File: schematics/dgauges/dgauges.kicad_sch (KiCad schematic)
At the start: 19 parts, among them J1 Conn_01x05_Female, U1 74HC595, U2 74HC595, U3 74HC595, U4 74HC595, U5 74HC595

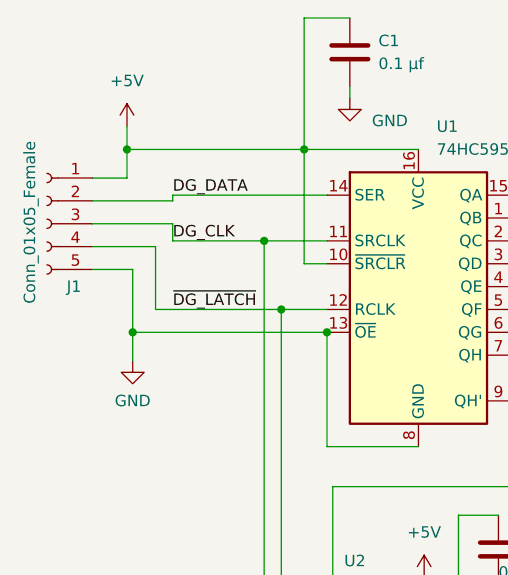
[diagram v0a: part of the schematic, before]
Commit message: SCH: dgauge => ust proper JST connector for J1
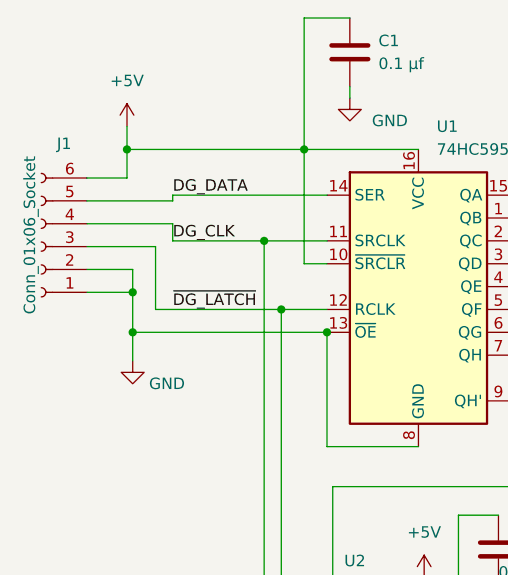
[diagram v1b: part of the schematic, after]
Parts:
- removed J1: Conn_01x05_Female, Connectors_JST:JST_EH_B05B-EH-A_05x2.50mm_Straight, symbol Connector:Conn_01x05_Female
- added J1: Conn_01x06_Socket, Connector_JST:JST_PH_B6B-PH-K_1x06_P2.00mm_Vertical, symbol Connector:Conn_01x06_Socket
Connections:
- net +5V: now also J1.6 (Pin_6)
- net DG_CLK: now also J1.4 (Pin_4)
- net DG_DATA: now also J1.5 (Pin_5)
- net GND: now also J1.1 (Pin_1), J1.2 (Pin_2)
- net ~{DG_LATCH}: now also J1.3 (Pin_3)

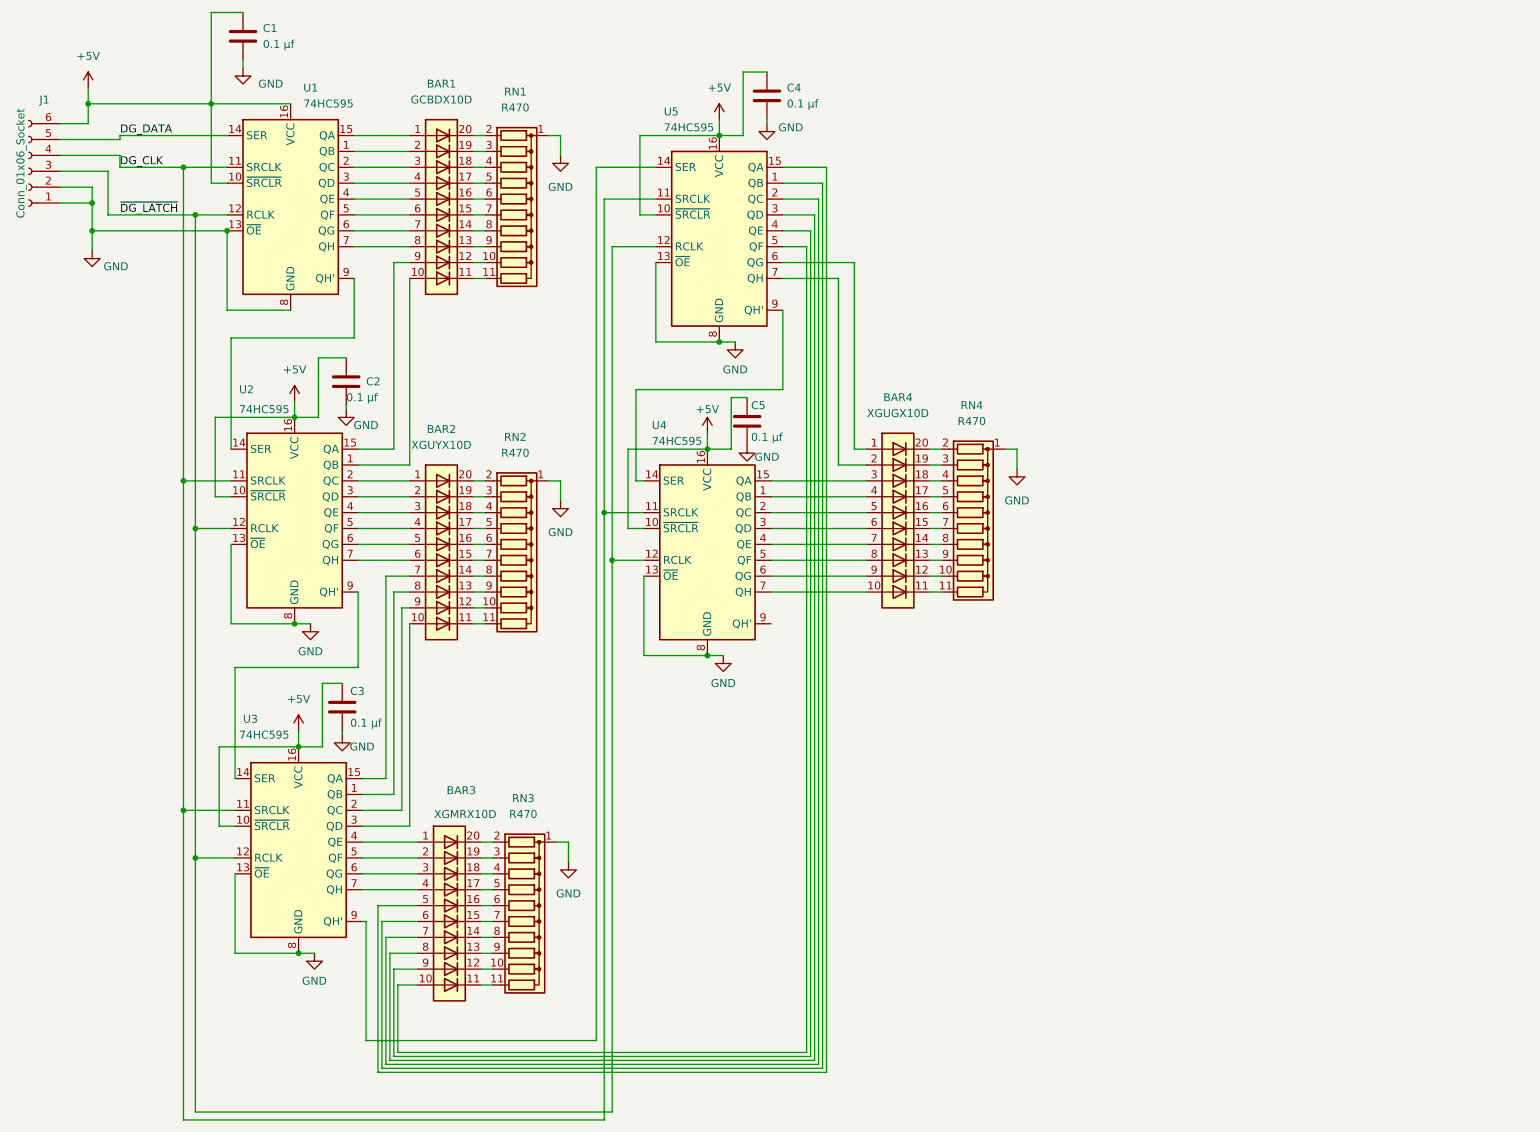
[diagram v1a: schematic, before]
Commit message: SCH: DGauges: route serial out to header for daisy-chaining
And add mounting holes
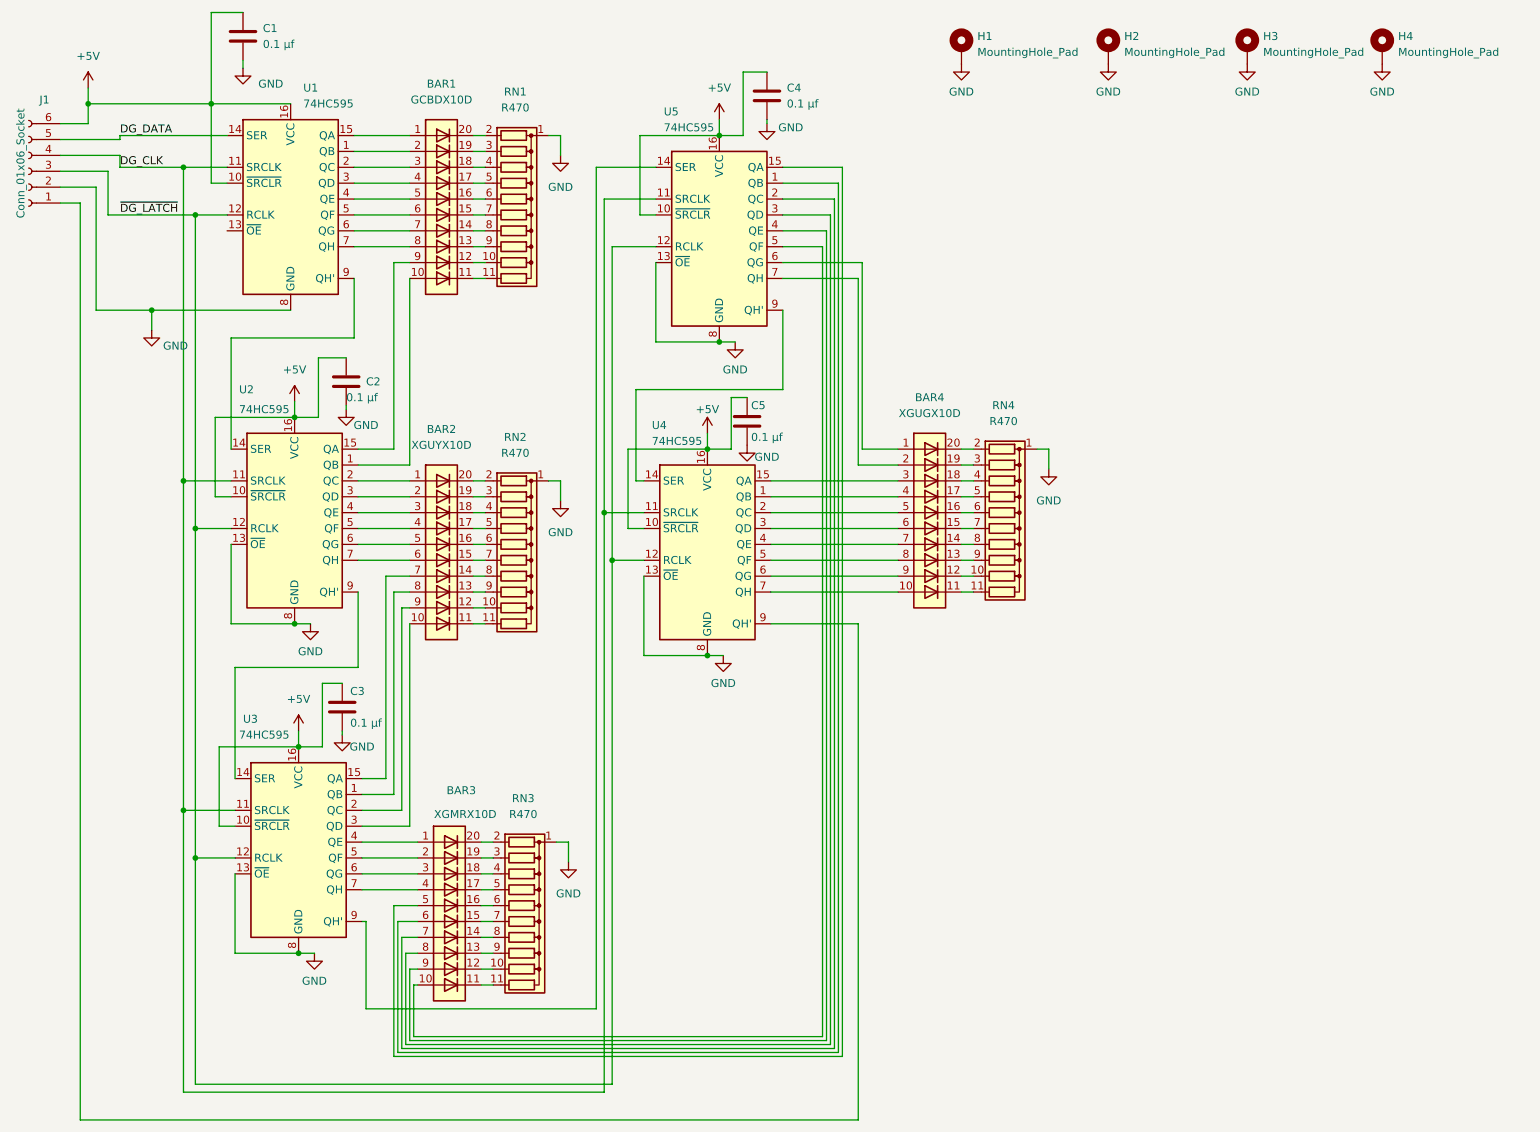
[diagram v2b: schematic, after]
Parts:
- added H1, H2, H3, H4: MountingHole_Pad, MountingHole:MountingHole_2.2mm_M2_ISO7380_Pad, symbol Mechanical:MountingHole_Pad
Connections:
- net GND: now also H1.1, H2.1, H3.1, H4.1; no longer J1.1 (Pin_1), U1.13 (~{OE})
- net at U4.9 (QH'): now also J1.1 (Pin_1)
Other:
- moved on the sheet: BAR4, RN4

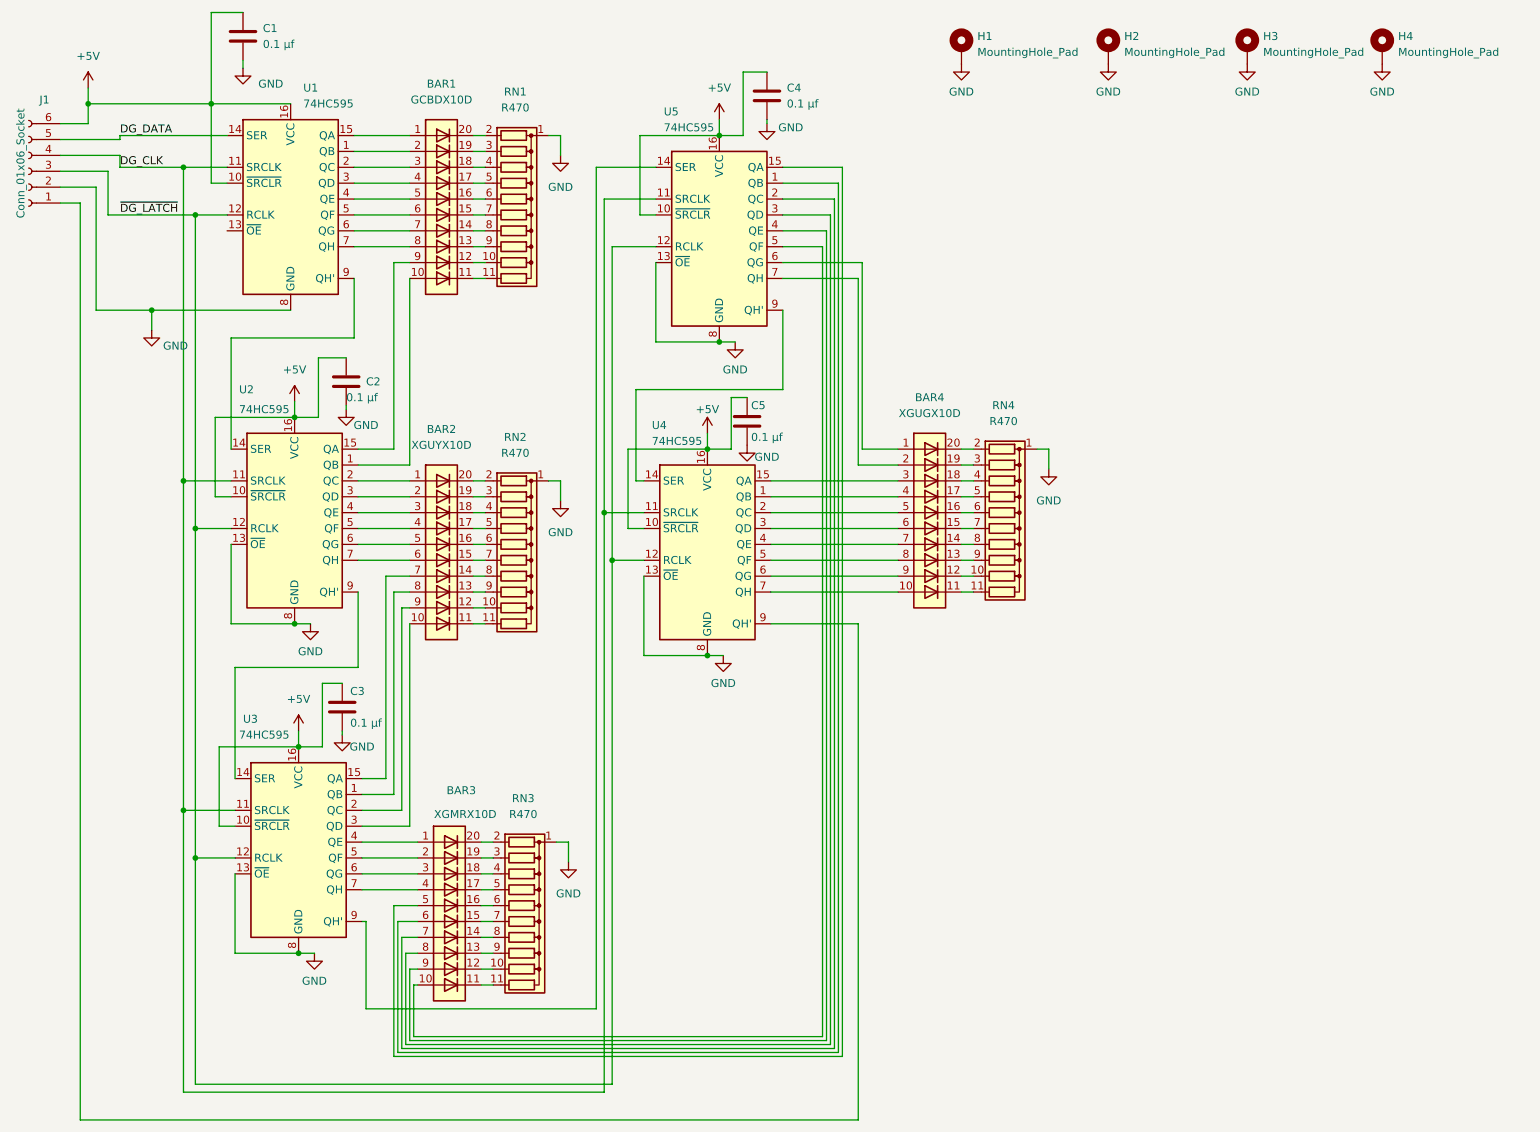
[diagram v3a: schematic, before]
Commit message: SCH: dgauges=> set res. values to get similar brightness on all bars
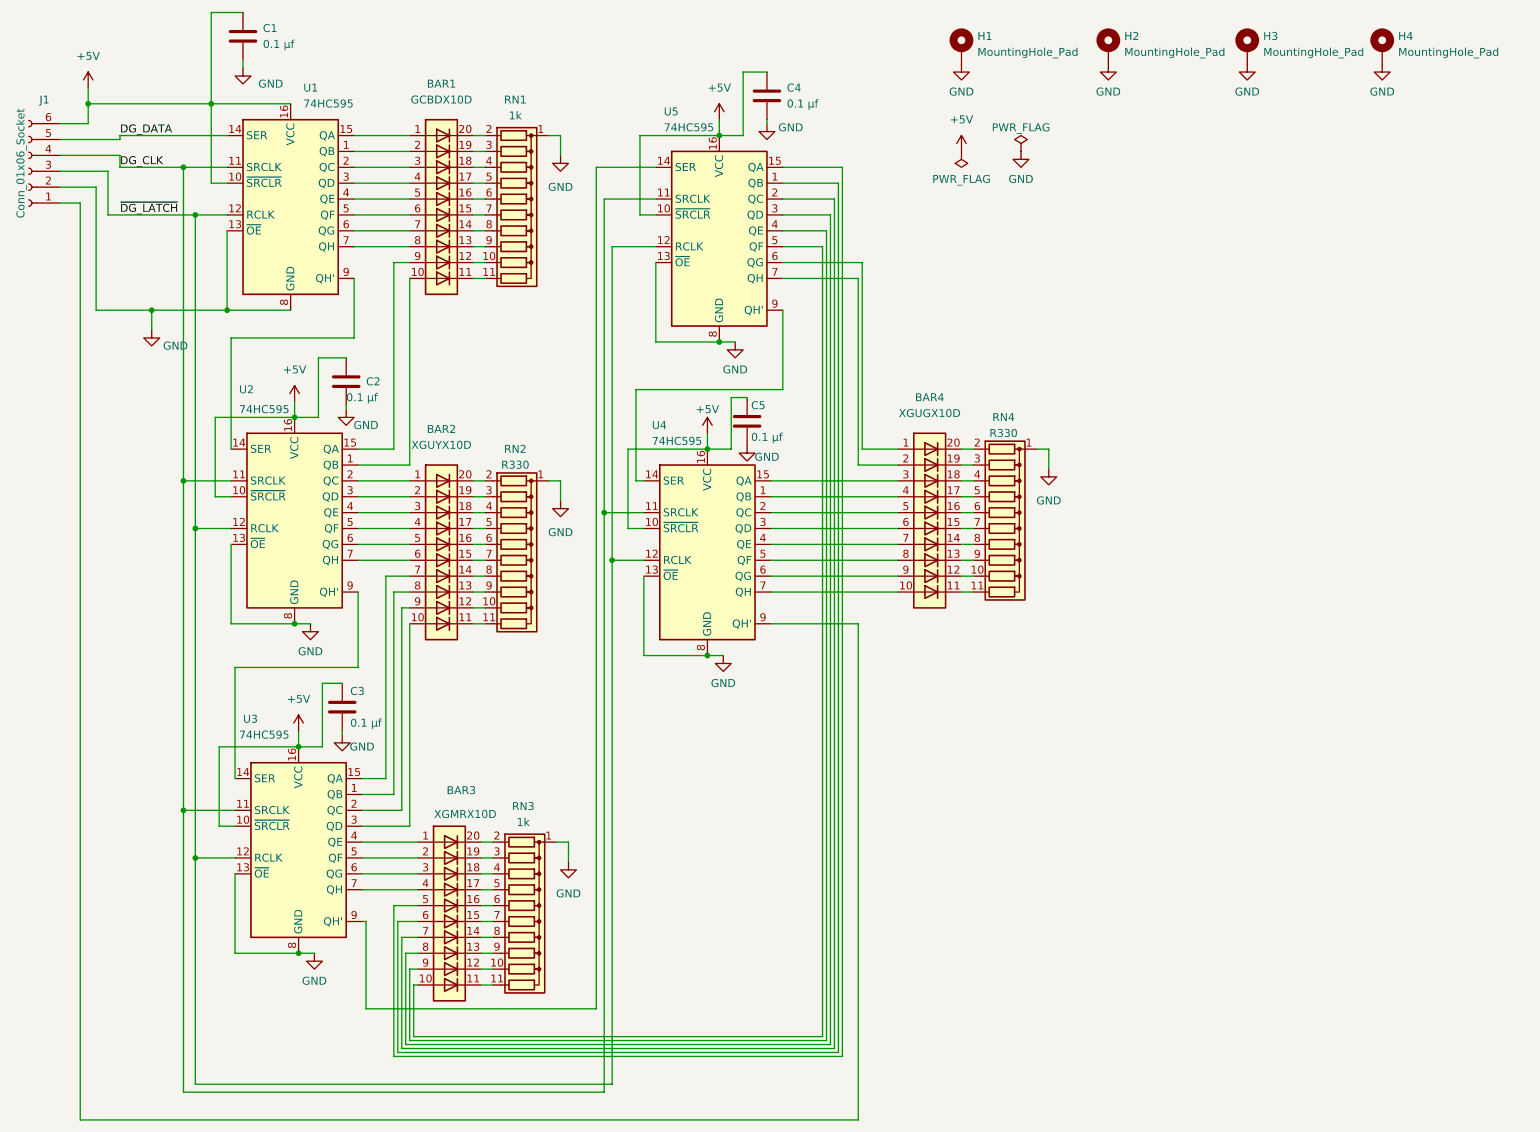
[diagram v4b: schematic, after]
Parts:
- RN1, RN3: value R470 -> 1k; digikey (none) -> 4611X-101-102LF-ND
- RN2, RN4: value R470 -> R330; digi-key (none) -> 4611X-101-331LF
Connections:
- net GND: now also U1.13 (~{OE})

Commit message: Sch: gauges: add one for xenon
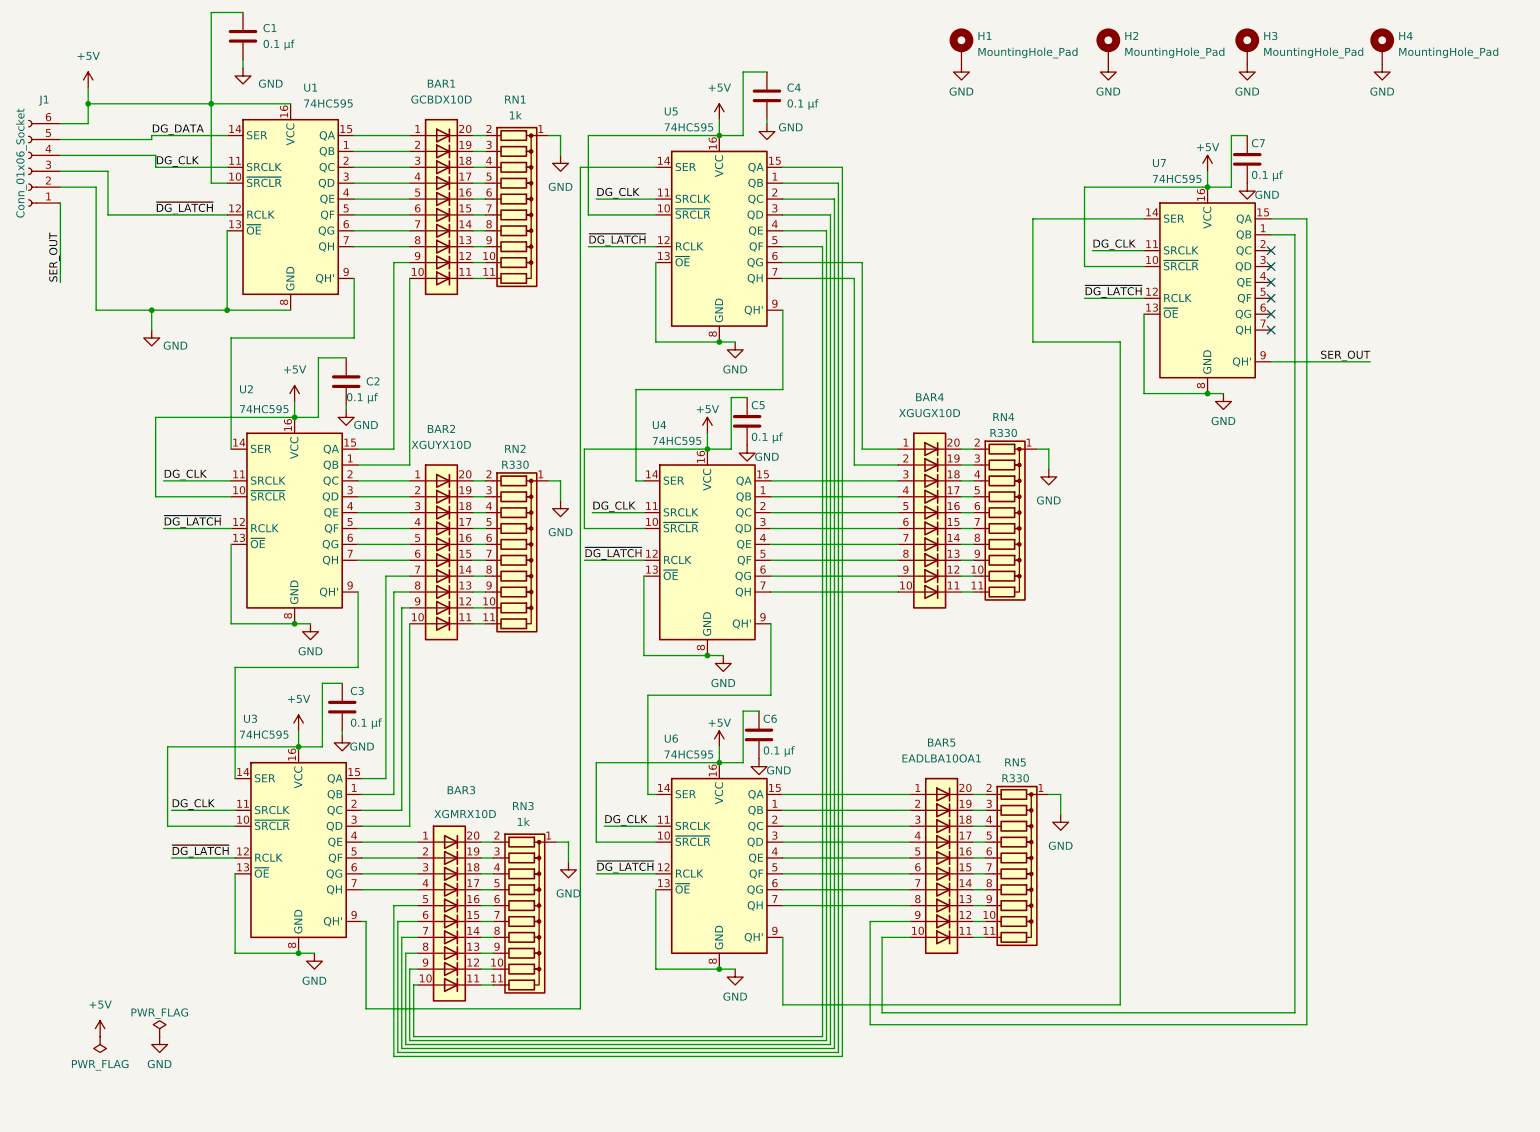
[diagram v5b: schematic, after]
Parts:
- added BAR5: EADLBA10OA1, Display:HDSP-4832, symbol LED:HDSP-4832_2
- added C6, C7: 0.1 µf, Capacitor_THT:C_Disc_D4.3mm_W1.9mm_P5.00mm, symbol Device:C
- added RN5: R330, Resistor_THT:R_Array_SIP11, symbol Device:R_Network10
- added U6, U7: 74HC595, Package_DIP:DIP-16_W7.62mm, symbol 74xx:74HC595
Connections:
- net +5V: now also C6.1, C7.1, U6.10 (~{SRCLR}), U6.16 (VCC), U7.10 (~{SRCLR}), U7.16 (VCC)
- net DG_CLK: now also U6.11 (SRCLK), U7.11 (SRCLK)
- net GND: now also C6.2, C7.2, RN5.1 (common), U6.13 (~{OE}), U6.8 (GND), U7.13 (~{OE}), U7.8 (GND)
- net ~{DG_LATCH}: now also U6.12 (RCLK), U7.12 (RCLK)
- net at U4.9 (QH'): now also U6.14 (SER); no longer J1.1 (Pin_1)
- new net: BAR5.10 (A), U7.1 (QB)
- new net: U6.9 (QH'), U7.14 (SER)
- new net: BAR5.9 (A), U7.15 (QA)
- new net: BAR5.2 (A), U6.1 (QB)
- new net: BAR5.1 (A), U6.15 (QA)
- new net: BAR5.3 (A), U6.2 (QC)
- new net: BAR5.4 (A), U6.3 (QD)
- new net: BAR5.5 (A), U6.4 (QE)
- new net: BAR5.6 (A), U6.5 (QF)
- new net: BAR5.7 (A), U6.6 (QG)
- new net: BAR5.8 (A), U6.7 (QH)
- new net: BAR5.12 (K), RN5.10 (R9)
- new net: BAR5.11 (K), RN5.11 (R10)
- new net: BAR5.20 (K), RN5.2 (R1)
- new net: BAR5.19 (K), RN5.3 (R2)
- new net: BAR5.18 (K), RN5.4 (R3)
- new net: BAR5.17 (K), RN5.5 (R4)
- new net: BAR5.16 (K), RN5.6 (R5)
- new net: BAR5.15 (K), RN5.7 (R6)
- new net: BAR5.14 (K), RN5.8 (R7)
- new net: BAR5.13 (K), RN5.9 (R8)
- new net SER_OUT: J1.1 (Pin_1), U7.9 (QH')
- no-connect marks 0 -> 6
